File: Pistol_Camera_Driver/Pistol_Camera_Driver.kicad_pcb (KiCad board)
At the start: 2 copper layers, 95.8 x 38.7 mm, 56 parts, among them J1 Screw_Terminal_01x02, J10 Bluetooth, J2 Objective, J3 Screw_Terminal_01x02, J4 Screw_Terminal_01x02, J5 SONAR, J6 Joystick, J7 Screw_Terminal_01x02, J8 Screw_Terminal_01x04, J9 Screw_Terminal_01x02, U1 LM7805_TO220, U10 RS0101YH6, U11 LDD-700L, U2 LM317_TO-263, U3 Raspberri_Pi_Pico, U4 DRV8834PWP, U5 DRV8834PWP, U6 RS0101YH6, U7 LDD-700L, U8 RS0101YH6, U9 LDD-700L

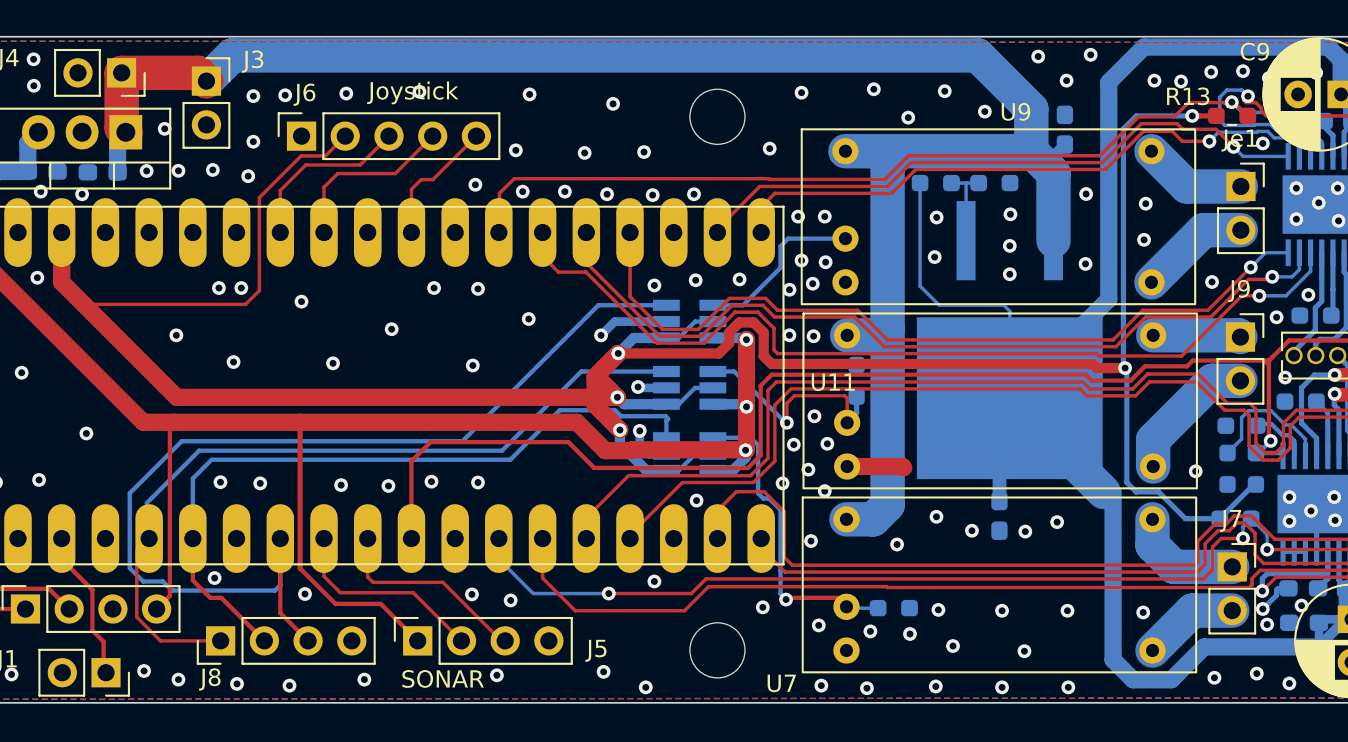
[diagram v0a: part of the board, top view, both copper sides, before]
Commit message: v1.5 2 reserve connectors were added, cosmetical changes
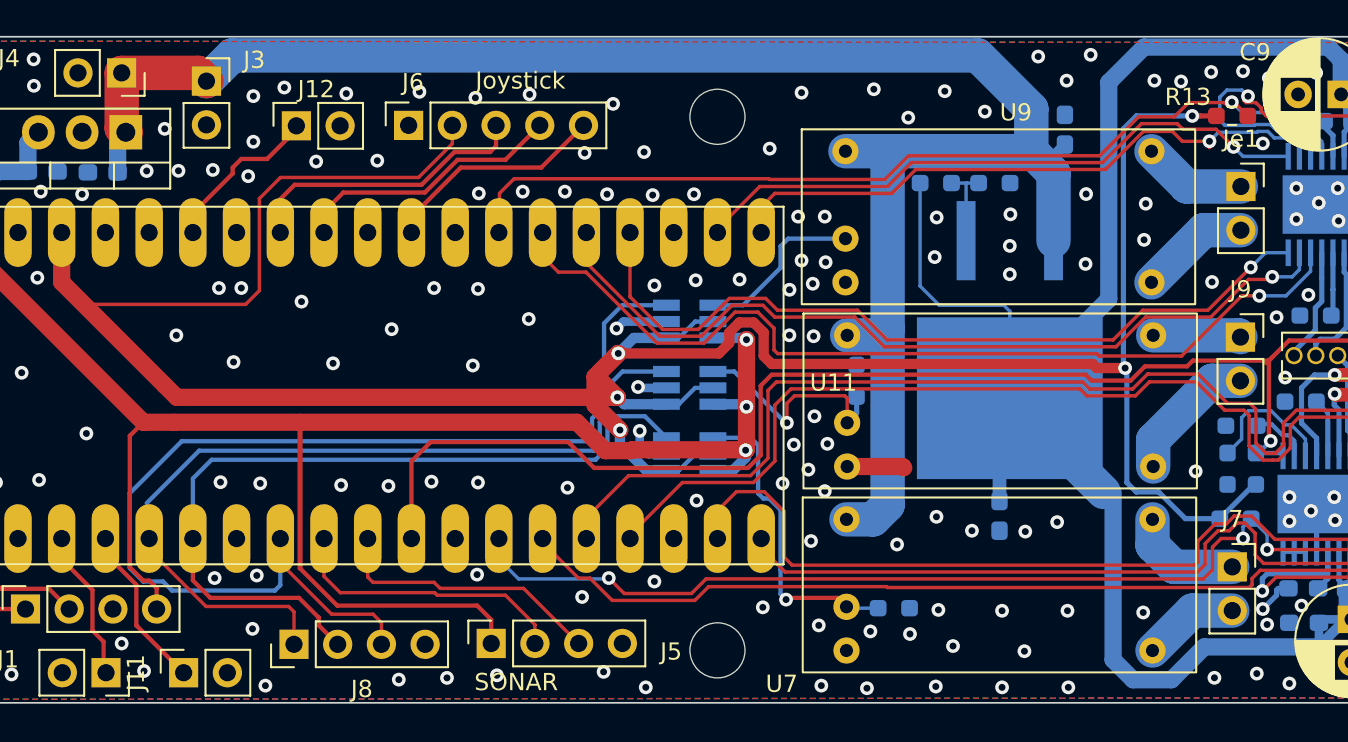
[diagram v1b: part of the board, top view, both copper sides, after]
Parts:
- added J11: Screw_Terminal_01x02, Connector_PinSocket_2.54mm:PinSocket_1x02_P2.54mm_Vertical, F.Cu at (94.2, 61.3)
- added J12: Screw_Terminal_01x02, Connector_PinSocket_2.54mm:PinSocket_1x02_P2.54mm_Vertical, F.Cu at (100.7, 29.5)
- moved J6 6.25 mm to (107.2, 29.5)
- moved J5 4.27 mm to (112.0, 59.6)
- moved J8 4.26 mm to (100.6, 59.6)
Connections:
- U3 pad 34: unconnected-(U3-Pad34) -> Reserve2
- U3 pad 5: unconnected-(U3-Pad5) -> Reserve1
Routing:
- net Reserve1: track 0.00 -> 9.68 mm
- net Reserve2: track 0.00 -> 9.57 mm
- net +3V3: track 161.9 -> 169.0 mm
- net VarY: track 10.1 -> 17.0 mm
- net PWM_WHITE: track 60.5 -> 67.4 mm
- net +5V: track 101.2 -> 107.4 mm
- net VarX: track 10.2 -> 15.8 mm
- net SW: track 7.56 -> 13.1 mm
- net TRIG: track 11.7 -> 16.7 mm
- net ECHO: track 11.8 -> 16.1 mm
- net PWM_UV: track 42.1 -> 46.4 mm
- net PWM_RED: track 44.0 -> 47.5 mm
- net nEN1: track 73.9 -> 72.2 mm
- net GND: track 19.2 -> 18.2 mm, vias 193 -> 197

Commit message: v1.7 ready 2 send
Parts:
- J1: value Screw_Terminal_01x02 -> Strobe
- J11, J12: value Screw_Terminal_01x02 -> reserve
- J8: value Screw_Terminal_01x04 -> test
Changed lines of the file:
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@@
       (effects (font (size 1 1) (thickness 0.15)))
     )
-    (fp_text value "Screw_Terminal_01x02" (at 0 5.31 90) (layer "F.Fab") hide
+    (fp_text value "reserve" (at -0.9 7.85 180) (layer "F.SilkS")
       (effects (font (size 1 1) (thickness 0.15)))
     )
@@
       (effects (font (size 1 1) (thickness 0.15)))
     )
-    (fp_text value "Screw_Terminal_01x02" (at 3.125 1.1 180) (layer "F.SilkS") hide
+    (fp_text value "Strobe" (at 0.6 6.34 180) (layer "F.SilkS")
       (effects (font (size 1 1) (thickness 0.15)))
     )
@@
       (effects (font (size 1 1) (thickness 0.15)))
     )
-    (fp_text value "SONAR" (at -2.25 1.45 180) (layer "F.SilkS")
+    (fp_text value "SONAR" (at 2.4 8.38 180) (layer "F.SilkS")
       (effects (font (size 1 1) (thickness 0.15)))
     )
@@
       (effects (font (size 1 1) (thickness 0.15)))
     )
-    (fp_text value "Screw_Terminal_01x02" (at 0 5.31 90) (layer "F.Fab")
+    (fp_text value "reserve" (at 3.825 2 180) (layer "F.Fab")
       (effects (font (size 1 1) (thickness 0.15)))
     )
@@
     (property "Sheetname" "")
     (attr through_hole)
-    (fp_text reference "J8" (at -2.6 3.94 180) (layer "F.SilkS")
-      (effects (font (size 1 1) (thickness 0.15)))
-    )
-    (fp_text value "Screw_Terminal_01x04" (at -3 1.2) (layer "F.SilkS") hide
+    (fp_text reference "J8" (at 2.55 4.94 180) (layer "F.SilkS")
+      (effects (font (size 1 1) (thickness 0.15)))
+    )
+    (fp_text value "test" (at 2.65 7.94) (layer "F.SilkS")
       (effects (font (size 1 1) (thickness 0.15)))
     )
@@
     (pts (xy 172.4 24.35) (xy 172.4 63.05))
     (height -5.45)
-    (gr_text "38.7000 мм" (at 176.7 43.7 90) (layer "Dwgs.User")
+    (gr_text "38,7000 мм" (at 176.7 43.7 90) (layer "Dwgs.User")
       (effects (font (size 1 1) (thickness 0.15)))
     )
@@
     (pts (xy 79.445 29) (xy 125.165 29))
     (height -6.75)
-    (gr_text "45.7200 мм" (at 102.305 21.1) (layer "Dwgs.User")
+    (gr_text "45,7200 мм" (at 102.305 21.1) (layer "Dwgs.User")
       (effects (font (size 1 1) (thickness 0.15)))
     )
@@
     (pts (xy 79.445 29) (xy 169.445 29))
     (height -10)
-    (gr_text "90.0000 мм" (at 124.445 17.85) (layer "Dwgs.User")
+    (gr_text "90,0000 мм" (at 124.445 17.85) (layer "Dwgs.User")
       (effects (font (size 1 1) (thickness 0.15)))
     )
@@
     (pts (xy 76.65 63.1) (xy 172.45 63.05))
     (height 8.800155)
-    (gr_text "95.8000 мм" (at 124.553993 70.725154 0.02990384881) (layer "Dwgs.User")
+    (gr_text "95,8000 мм" (at 124.553993 70.725154 0.02990384881) (layer "Dwgs.User")
       (effects (font (size 1 1) (thickness 0.15)))
     )
@@
     (pts (xy 79.445 29) (xy 79.445 60))
     (height 8.145)
-    (gr_text "31.0000 мм" (at 70.15 44.5 90) (layer "Dwgs.User")
+    (gr_text "31,0000 мм" (at 70.15 44.5 90) (layer "Dwgs.User")
       (effects (font (size 1 1) (thickness 0.15)))
     )
@@
   (via (at 168.650452 33.093075) (size 0.8) (drill 0.4) (layers "F.Cu" "B.Cu") (free) (net 2))
   (via (at 158.392757 61.925607) (size 0.8) (drill 0.4) (layers "F.Cu" "B.Cu") (free) (net 2))
-  (via (at 81.55 61.8) (size 0.8) (drill 0.4) (layers "F.Cu" "B.Cu") (free) (net 2))
+  (via (at 82.2 60.1) (size 0.8) (drill 0.4) (layers "F.Cu" "B.Cu") (free) (net 2))
   (via (at 161.2 33.15) (size 0.8) (drill 0.4) (layers "F.Cu" "B.Cu") (free) (net 2))
   (via (at 131.2 62.05) (size 0.8) (drill 0.4) (layers "F.Cu" "B.Cu") (free) (net 2))
@@
   (via (at 85.75 50.1) (size 0.8) (drill 0.4) (layers "F.Cu" "B.Cu") (free) (net 2))
   (via (at 142.185896 34.66596) (size 0.8) (drill 0.4) (layers "F.Cu" "B.Cu") (free) (net 2))
-  (via (at 84.15 61.4) (size 0.8) (drill 0.4) (layers "F.Cu" "B.Cu") (free) (net 2))
+  (via (at 84.9 60.4) (size 0.8) (drill 0.4) (layers "F.Cu" "B.Cu") (free) (net 2))
   (via (at 126.45 38.45) (size 0.8) (drill 0.4) (layers "F.Cu" "B.Cu") (free) (net 2))
   (via (at 130.75 41.75) (size 0.8) (drill 0.4) (layers "F.Cu" "B.Cu") (free) (net 2))

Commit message: Auto stash before merge of "main" and "origin/main"
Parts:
- removed the R9 at (167.1, 35.8)
- R13: value R -> 10 k
- moved R9 2.07 mm to (166.7, 36.6), turned to -90 degrees
- moved R10 0.92 mm to (168.3, 36.7)
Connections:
- U3 pad 36: unconnected-(U3-Pad36) -> +3V3
- U3 pad 37: +3V3 -> unconnected-(U3-Pad37)
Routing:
- net +3.3VP: track 138.3 -> 117.0 mm
- net +3V3: track 169.0 -> 161.8 mm
- net Net-(R10-Pad2): track 7.71 -> 6.56 mm
- net Net-(R9-Pad2): track 3.23 -> 3.73 mm

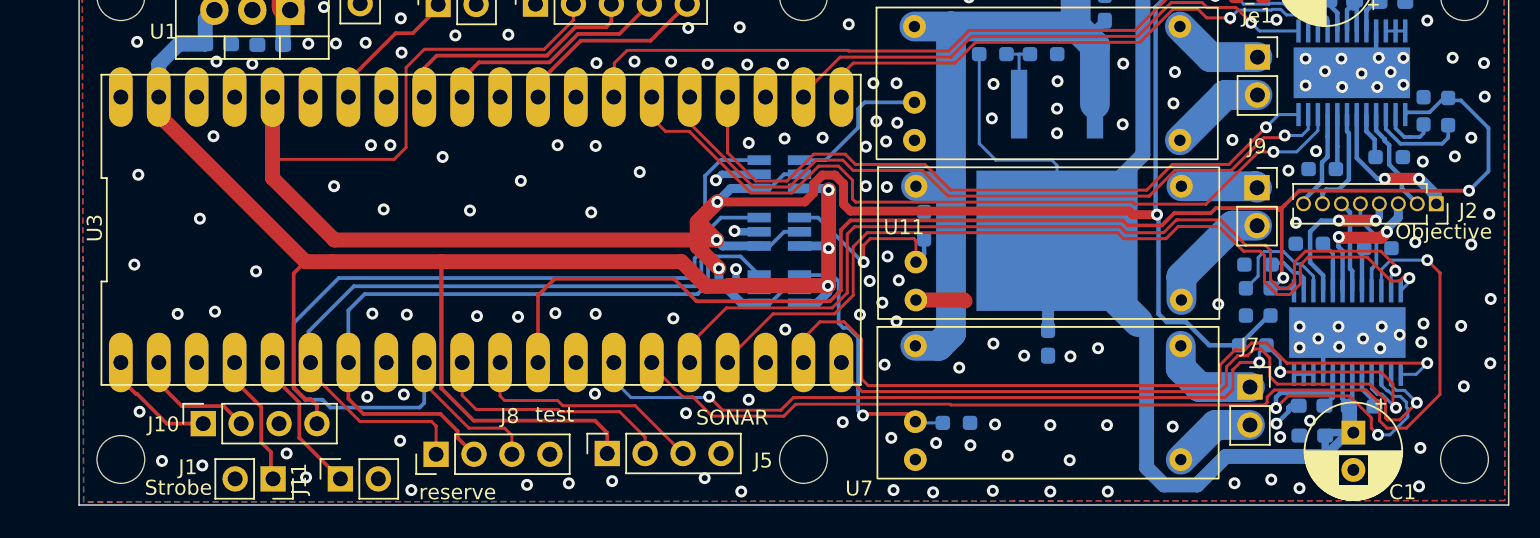
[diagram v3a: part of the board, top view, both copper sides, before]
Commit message: v2.0 Circuit, PCB were corrected
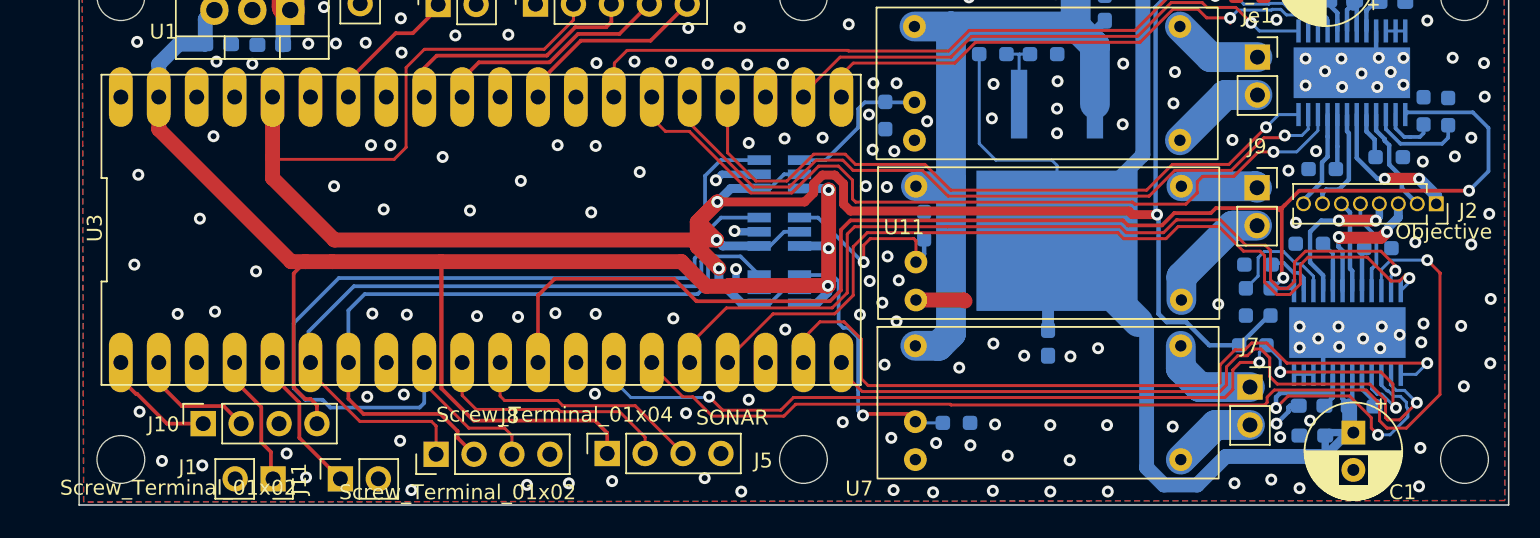
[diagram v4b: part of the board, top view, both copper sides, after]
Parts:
- added R16: R, Resistor_SMD:R_0603_1608Metric_Pad0.98x0.95mm_HandSolder, B.Cu at (130.7, 37.0)
- J1: value Strobe -> Screw_Terminal_01x02
- J11, J12: value reserve -> Screw_Terminal_01x02
- J8: value test -> Screw_Terminal_01x04
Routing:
- net MOTORS_nSLEEP: track 93.2 -> 92.6 mm
- net +5V: track 107.4 -> 108.0 mm

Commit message: v2.2 i2C ToА proto
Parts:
- added J13: I2C, Connector_PinSocket_2.54mm:PinSocket_1x04_P2.54mm_Vertical, F.Cu at (93.4, 67.4)
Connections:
- U3 pad 10: TRIG -> PWM_RED
- U3 pad 11: ECHO -> PWM_UV
- U3 pad 6: PWM_RED -> SDA
- U3 pad 7: PWM_UV -> SCL
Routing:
- net PWM_RED: track 47.5 -> 64.2 mm
- net TRIG: track 16.7 -> 0.00 mm
- net PWM_UV: track 46.4 -> 62.5 mm
- net ECHO: track 16.1 -> 0.00 mm

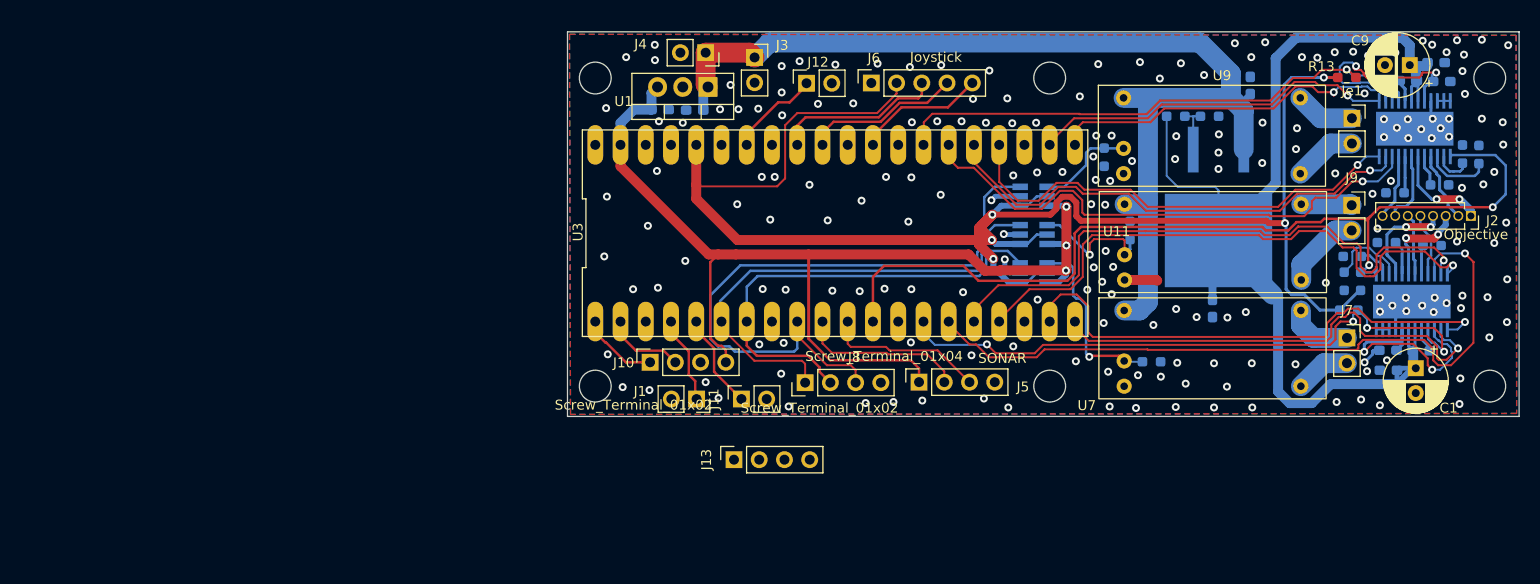
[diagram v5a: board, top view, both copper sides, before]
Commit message: v2.3 Circuit was changed. (4 LEDs, Solenoid driver)
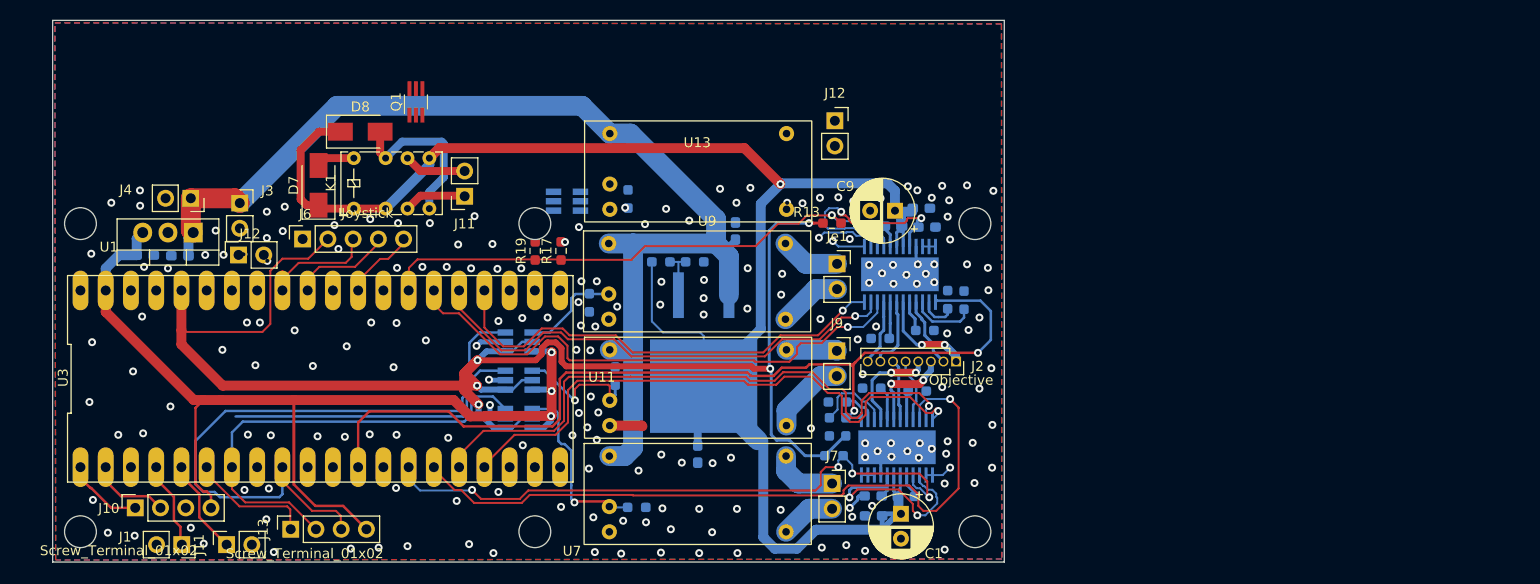
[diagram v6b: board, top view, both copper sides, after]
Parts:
- removed J5: SONAR, Connector_PinSocket_2.54mm:PinSocket_1x04_P2.54mm_Vertical
- removed J8: Screw_Terminal_01x04, Connector_PinHeader_2.54mm:PinHeader_1x04_P2.54mm_Vertical
- added D7: CDBA3100-HF, Diode_SMD:D_SMA, F.Cu at (51.6, 39.8)
- added D8: CDBA3100-HF, Diode_SMD:D_SMA, F.Cu at (55.8, 34.4)
- added J11: Screw_Terminal_01x02, Connector_PinSocket_2.54mm:PinSocket_1x02_P2.54mm_Vertical, F.Cu at (66.3, 40.9)
- added J12: Screw_Terminal_01x02, Connector_PinSocket_2.54mm:PinSocket_1x02_P2.54mm_Vertical, F.Cu at (103.5, 33.3)
- added K1: IM03, Relay_THT:Relay_DPDT_AXICOM_IMSeries_Pitch5.08mm, F.Cu at (55.1, 42.1)
- added Q1: FFB2222A, Package_TO_SOT_SMD:SOT-363_SC-70-6_Handsoldering, F.Cu at (61.4, 31.4)
- added R17: 1k, Resistor_SMD:R_0603_1608Metric_Pad0.98x0.95mm_HandSolder, F.Cu at (76.0, 46.4)
- added R18: 10k, Resistor_SMD:R_0603_1608Metric_Pad0.98x0.95mm_HandSolder, B.Cu at (82.7, 41.2)
- added R19: 1k, Resistor_SMD:R_0603_1608Metric_Pad0.98x0.95mm_HandSolder, F.Cu at (73.4, 46.4)
- added U12: RS0101YH6, Package_TO_SOT_SMD:SOT-23-6_Handsoldering, B.Cu at (76.6, 41.4)
- added U13: LDD-700L, Shield_Emergent:LDD-700L, F.Cu at (80.9, 34.6)
- R14, R15: value R -> 10k
- moved J12 59.7 mm to (43.5, 46.8)
- moved J6 59.3 mm to (50.0, 45.2)
- moved C10 53.8 mm to (112.2, 42.1)
- moved C12 53.8 mm to (112.8, 44.0)
- moved C6 53.8 mm to (89.8, 66.8)
- moved C7 53.8 mm to (110.8, 71.1)
- moved C9 53.8 mm to (109.6, 42.4)
- moved J2 53.8 mm to (115.8, 57.5)
- moved J9 53.8 mm to (103.8, 56.5)
- moved R11 53.8 mm to (112.6, 54.4)
- moved R16 53.8 mm to (78.8, 51.6)
- moved R2 53.8 mm to (103.8, 61.6)
- moved R4 53.8 mm to (103.0, 64.1)
- moved R5 53.8 mm to (107.2, 60.2)
- moved REF** 53.8 mm to (73.4, 74.7)
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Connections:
- U3 pad 19: M0_1 -> unconnected-(U3-Pad19)
- U3 pad 20: M1_1 -> unconnected-(U3-Pad20)
- U3 pad 21: M1_2 -> Solenoid_DIR
- U3 pad 22: M0_2 -> Solenoid_ON
- U3 pad 34: Reserve2 -> unconnected-(U3-Pad34)
- U3 pad 5: Reserve1 -> unconnected-(U3-Pad5)
- U4 pad 13: M0_1 -> GND
- U4 pad 14: M1_1 -> GND
- U5 pad 13: M0_2 -> GND
- U5 pad 14: M1_2 -> GND
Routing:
- net +3.3VP: track 117.0 -> 179.8 mm, vias 0 -> 1
- net PWM_UV: track 62.5 -> 0.00 mm
- net M0_1: track 51.7 -> 0.00 mm, vias 1 -> 0
- net M1_1: track 48.6 -> 0.00 mm, vias 1 -> 0
- net SCL: track 0.00 -> 46.1 mm
- net M0_2: track 36.7 -> 0.00 mm, vias 1 -> 0
- net M1_2: track 36.5 -> 0.00 mm, vias 1 -> 0
- net PWM_RED: track 64.2 -> 30.8 mm
- net Net-(D8-Pad2): track 0.00 -> 16.6 mm
- net GND: track 18.2 -> 30.9 mm, vias 197 -> 200
- net SDA: track 0.00 -> 12.4 mm
- net Reserve2: track 9.37 -> 0.00 mm
- net +12V: track 107.9 -> 114.7 mm
- net +3V3: track 161.8 -> 155.4 mm
- net Net-(J11-Pad1): track 0.00 -> 6.31 mm
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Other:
- board size 95.8 x 38.7 mm -> 95.8 x 54.5 mm

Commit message: v2.4 some nets were routed
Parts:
- Q1: value FFB2222A -> locked
- moved Q1 17.3 mm to (74.6, 42.6), turned to 0 degrees
- moved REF** 8.00 mm to (73.4, 35.6)
- moved REF** 8.00 mm to (27.6, 35.6)
- moved REF** 8.00 mm to (117.6, 35.6)
- moved R18 3.78 mm to (79.0, 40.6)
- moved U12 1.28 mm to (75.6, 40.6)
- moved J12 0.84 mm to (103.2, 34.1)
- moved D8 0.20 mm to (55.8, 34.2)
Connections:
- U3 pad 34: unconnected-(U3-Pad34) -> PWM_IR
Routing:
- net +5V: track 103.5 -> 153.7 mm, vias 3 -> 4
- net PWM_IR: track 0.00 -> 39.1 mm
- net SCL: track 46.1 -> 12.3 mm
- net PWM_UV: track 0.00 -> 24.0 mm
- net Net-(D8-Pad2): track 16.6 -> 40.4 mm, vias 0 -> 1
- net Net-(D7-Pad2): track 3.86 -> 26.6 mm
- net +3V3: track 155.4 -> 177.3 mm
- net PWM_WHITE: track 67.4 -> 47.2 mm
- net unconnected-(U3-Pad5): track 0.00 -> 9.68 mm
- net Reserve1: track 9.68 -> 0.00 mm
- net Net-(D10-Pad1): track 0.00 -> 7.48 mm
- net Net-(D9-Pad2): track 0.00 -> 4.73 mm
- net Net-(Q1-Pad5): track 0.00 -> 4.53 mm
- net Net-(Q1-Pad2): track 0.00 -> 4.50 mm
- net GND: track 30.9 -> 35.3 mm, vias 200 -> 201
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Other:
- board size 95.8 x 54.5 mm -> 95.8 x 46.1 mm
